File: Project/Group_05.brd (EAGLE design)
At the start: 100 x 80 mm, 29 parts, among them J1 POWER_JACKPTH_LOCK, U1 +12v, U3 TCA9546A_SMD

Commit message: commit
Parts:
- moved D1 144.8 mm to (91.4, 14.0)
- moved R1 142.0 mm to (96.5, 10.2), turned to 90 degrees
- moved J6 130.6 mm to (96.5, 62.2), turned to 270 degrees
- moved J8 126.5 mm to (54.6, 3.81), turned to 90 degrees
- moved U$3 121.4 mm to (71.1, 43.2), turned to 90 degrees
- moved U$2 101.7 mm to (74.9, 2.54)
- moved U3 100.1 mm to (48.3, 57.1)
- moved R10 84.7 mm to (26.7, 11.4)
- moved C2 84.4 mm to (30.5, 69.8)
- moved U2 77.3 mm to (12.7, 11.4)
- moved C1 76.1 mm to (34.3, 74.9)
- moved J7 74.8 mm to (26.7, 77.5)
- moved J1 72.4 mm to (52.1, 26.7)
- moved C3 68.7 mm to (20.3, 74.9)
- moved R4 67.8 mm to (2.54, 35.6)
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
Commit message: Board commit
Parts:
- moved C1 80.7 mm to (72.4, 3.81), turned to 270 degrees
- moved U1 79.2 mm to (83.8, 19.1), turned to 180 degrees
- moved J8 76.4 mm to (34.3, 77.5), turned to 0 degrees
- moved C2 75.5 mm to (64.8, 2.54), turned to 270 degrees
- moved R1 72.8 mm to (24.1, 17.8), turned to 0 degrees
- moved U$2 72.0 mm to (25.2, 54.6), turned to 90 degrees
- moved D1 65.4 mm to (26.7, 22.9)
- moved C3 49.9 mm to (14.0, 25.4)
- moved J3 49.6 mm to (21.6, 77.5)
- moved J4 48.7 mm to (15.2, 77.5)
- moved J2 47.8 mm to (27.9, 77.5)
- moved J6 46.6 mm to (73.7, 21.6), turned to 180 degrees
- moved R11 40.9 mm to (38.1, 22.9), turned to 90 degrees
- moved U3 37.8 mm to (15.0, 39.3), turned to 180 degrees
- moved R2 36.8 mm to (3.81, 35.6), turned to 180 degrees
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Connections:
- removed net MUX_A0/2.3C: U$3.24
- removed net MUX_A1/2.3C: U$3.23
- removed net MUX_A2/2.3C: U$3.22
- removed net MUX_OUT/2.5C: U$3.21
- removed net N$10: R6.1, U3.12
- net I2C_SCL_3: now also R6.1, U3.12
- net MUX_A0/1.3C: now also U$3.24
- net MUX_A1/1.4C: now also U$3.23
- net MUX_A2/1.4C: now also U$3.22
- net MUX_OUT/1.4C: now also U$3.21
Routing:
- net 5V: track 0.00 -> 298.9 mm, vias 0 -> 7
- net I2C_SDA: track 0.00 -> 152.0 mm, vias 0 -> 1
- net I2C_SCL: track 0.00 -> 147.7 mm, vias 0 -> 2
- net GND: track 0.00 -> 146.8 mm, vias 0 -> 2
- net I2C_A2: track 0.00 -> 95.9 mm, vias 0 -> 2
- net I2C_SCL_2: track 0.00 -> 86.2 mm, vias 0 -> 3
- net I2C_SDA_0: track 0.00 -> 69.0 mm
- net MUX_A2/1.4C: track 0.00 -> 66.9 mm, vias 0 -> 3
- net I2C_A0: track 0.00 -> 66.6 mm, vias 0 -> 1
- net I2C_SCL_0: track 0.00 -> 64.1 mm, vias 0 -> 3
- net I2C_SCL_1: track 0.00 -> 62.9 mm
- net I2C_A1: track 0.00 -> 59.9 mm, vias 0 -> 1
- net S1: track 0.00 -> 56.4 mm
- net S2: track 0.00 -> 56.1 mm
- net I2C_SDA_1: track 0.00 -> 55.8 mm, vias 0 -> 4
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
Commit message: brd placement
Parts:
- removed U$3: CY8CKIT-059_TARGET_3, CY8KIT-059:CY8CKIT-059_TARGET_3
- added U$1: CY8CKIT-059_TARGET, CY8KIT-059:CY8CKIT-059_TARGET
- moved J7 91.4 mm to (61.0, 5.08), turned to 270 degrees
- moved J4 77.2 mm to (72.3, 25.4)
- moved R5 75.5 mm to (71.1, 20.3), turned to 270 degrees
- moved R4 71.7 mm to (74.9, 20.3), turned to 270 degrees
- moved C3 55.2 mm to (64.8, 3.81), turned to 90 degrees
- moved R7 53.4 mm to (57.1, 48.3), turned to 0 degrees
- moved R6 53.3 mm to (57.1, 50.8), turned to 0 degrees
- moved J5 53.2 mm to (53.3, 48.3), turned to 90 degrees
- moved J1 47.0 mm to (6.35, 1.27)
- moved S1 40.6 mm to (22.9, 11.4), turned to 0 degrees
- moved U1 39.0 mm to (47.0, 6.35), turned to 0 degrees
- moved C2 35.4 mm to (31.8, 15.2), turned to 90 degrees
- moved R3 29.2 mm to (20.3, 55.9)
- moved J3 28.2 mm to (25.4, 49.5), turned to 270 degrees
- moved U3 27.2 mm to (40.6, 48.3), turned to 0 degrees
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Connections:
- net 5V: now also U$1.26, U$1.27; no longer U$3.26, U$3.27
- net GND: now also U$1.25, U$1.28, U$1.52; no longer U$3.25, U$3.28, U$3.52
- net I2C_A0: now also U$1.6; no longer U$3.6
- net I2C_A1: now also U$1.7; no longer U$3.7
- net I2C_A2: now also U$1.8; no longer U$3.8
- net I2C_SCL: now also U$1.16; no longer U$3.16
- net I2C_SDA: now also U$1.15; no longer U$3.15
- net MUX_A0/1.3C: now also U$1.24; no longer U$3.24
- net MUX_A1/1.4C: now also U$1.23; no longer U$3.23
- net MUX_A2/1.4C: now also U$1.22; no longer U$3.22
- net MUX_OUT/1.4C: now also U$1.21; no longer U$3.21
- net N$1: now also U$1.37; no longer U$3.37
- net N$2: now also U$1.51; no longer U$3.51
- net N$5: now also U$1.36; no longer U$3.36
- net N$6: now also U$1.35; no longer U$3.35
- net N$7: now also U$1.34; no longer U$3.34
- net N$8: now also U$1.33; no longer U$3.33
- net N$9: now also U$1.32; no longer U$3.32
- net PHOTO_OUT: now also U$1.44; no longer U$3.44
- net TEMP_OUT: now also U$1.43; no longer U$3.43
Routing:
- net I2C_SDA: track 152.0 -> 22.0 mm
- net I2C_SCL: track 147.7 -> 22.7 mm, vias 2 -> 1
- net 5V: track 298.9 -> 204.8 mm, vias 7 -> 3
- net GND: track 146.8 -> 238.5 mm, vias 2 -> 5
- net I2C_A2: track 95.9 -> 11.7 mm, vias 2 -> 1
- net MUX_A2/1.4C: track 66.9 -> 15.3 mm, vias 3 -> 1
- net I2C_SDA_0: track 69.0 -> 19.6 mm
- net I2C_SCL_1: track 62.9 -> 16.7 mm
- net S1: track 56.4 -> 10.9 mm
- net I2C_SCL_0: track 64.1 -> 19.0 mm, vias 3 -> 0
- net S2: track 56.1 -> 11.2 mm
- net I2C_A0: track 66.6 -> 26.0 mm
- net I2C_SDA_1: track 55.8 -> 17.7 mm, vias 4 -> 0
- net I2C_SCL_3: track 49.9 -> 14.4 mm, vias 4 -> 2
- net I2C_A1: track 59.9 -> 27.2 mm
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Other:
- board size 100 x 80 mm -> 108.9 x 80 mm

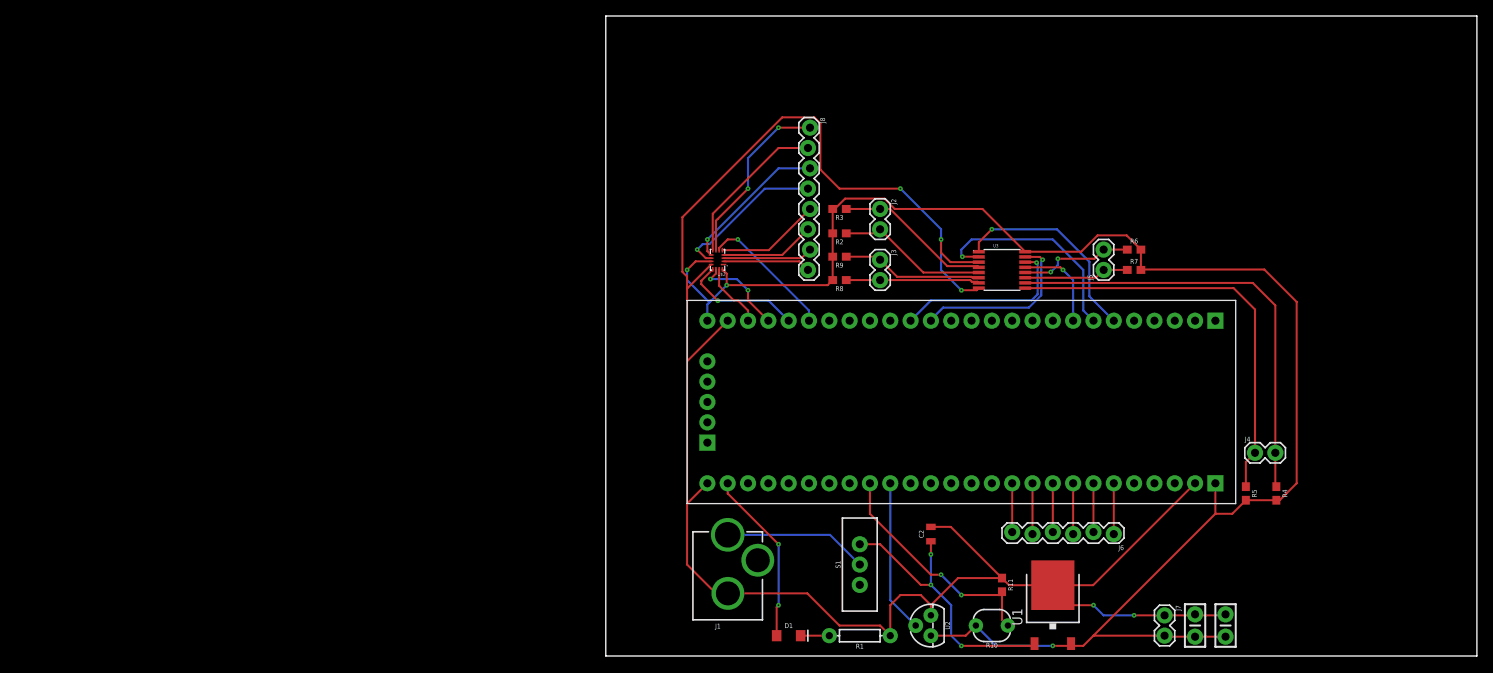
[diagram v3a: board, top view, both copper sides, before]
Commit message: Reduced dimensions
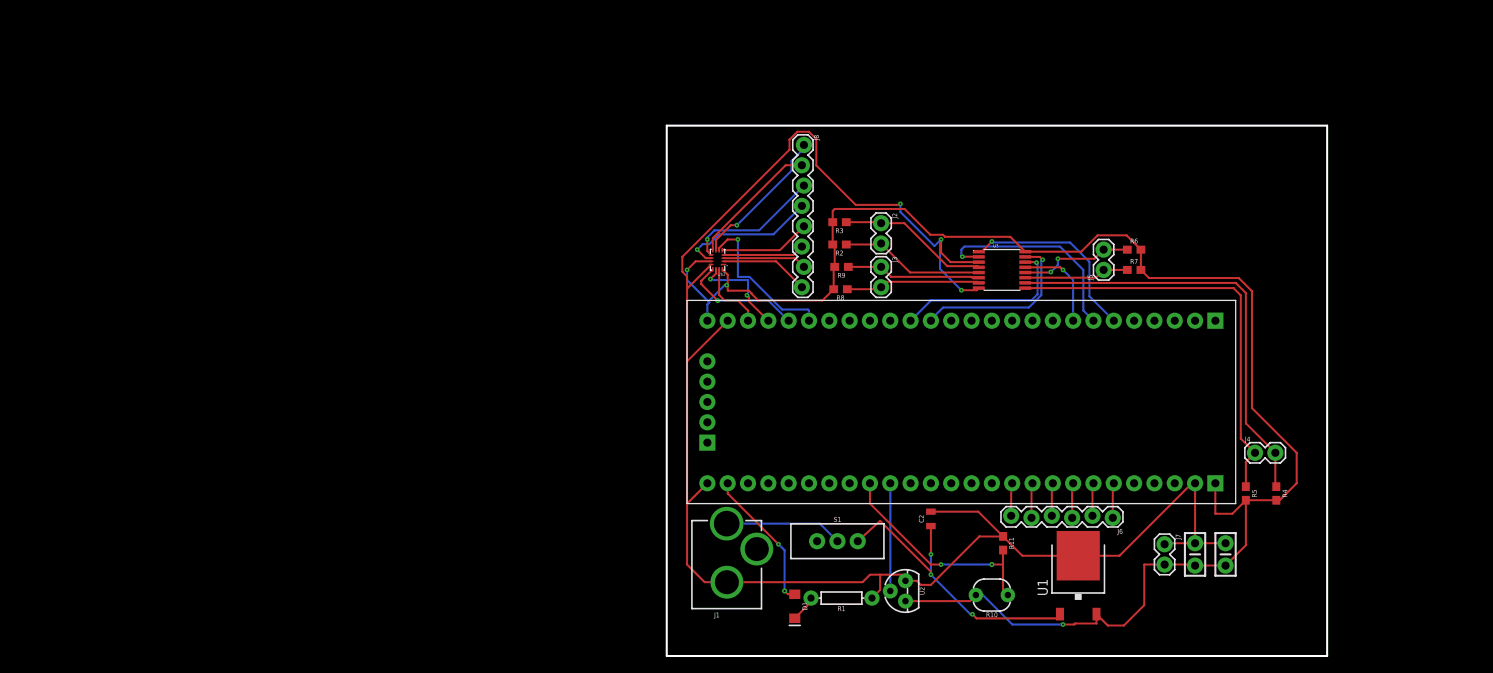
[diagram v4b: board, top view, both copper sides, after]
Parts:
- moved J7 8.89 mm to (61.0, 14.0)
- moved C1 8.89 mm to (68.6, 12.7)
- moved C3 8.89 mm to (64.8, 12.7)
- moved U2 5.36 mm to (28.6, 8.13)
- moved R1 5.23 mm to (20.6, 7.24)
- moved R11 5.21 mm to (40.8, 14.1)
- moved U1 4.86 mm to (50.2, 10.0)
- moved S1 4.04 mm to (20.1, 14.4), turned to 270 degrees
- moved R10 3.81 mm to (39.4, 7.62)
- moved D1 3.76 mm to (14.7, 6.22), turned to 270 degrees
- moved J8 2.29 mm to (15.7, 63.9)
- moved J6 2.04 mm to (54.5, 17.3)
- moved C2 1.90 mm to (31.8, 17.1)
- moved J2 1.78 mm to (25.5, 54.1)
- moved R3 1.65 mm to (20.3, 54.2)
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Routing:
- net GND: track 238.5 -> 224.5 mm, vias 5 -> 3
- net TEMP_OUT: track 19.1 -> 13.5 mm
- net S8: track 22.5 -> 18.2 mm, vias 2 -> 1
- net S7: track 19.9 -> 16.4 mm
- net N$3: track 18.0 -> 14.8 mm
- net N$2: track 21.8 -> 18.5 mm
- net 12V: track 34.9 -> 38.1 mm
- net MUX_OUT/1.4C: track 16.9 -> 19.6 mm
- net 5V: track 204.8 -> 202.5 mm
- net N$1: track 6.10 -> 4.12 mm
- net N$8: track 6.10 -> 4.12 mm
- net N$6: track 6.10 -> 4.12 mm
- net N$9: track 6.35 -> 4.37 mm
- net N$7: track 6.35 -> 4.37 mm
- net N$5: track 6.35 -> 4.37 mm
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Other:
- board size 108.9 x 80 mm -> 82.5 x 66.3 mm

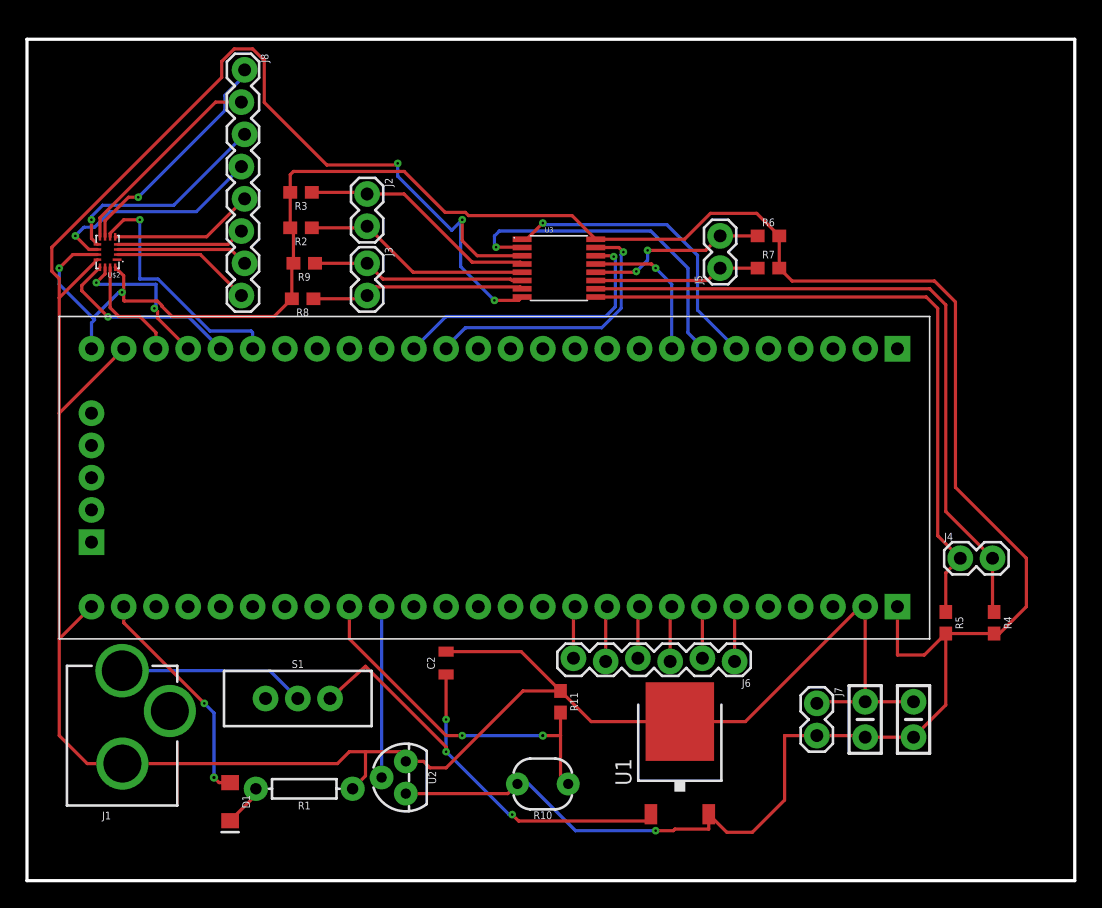
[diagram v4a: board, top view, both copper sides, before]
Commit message: Holes, copper pour
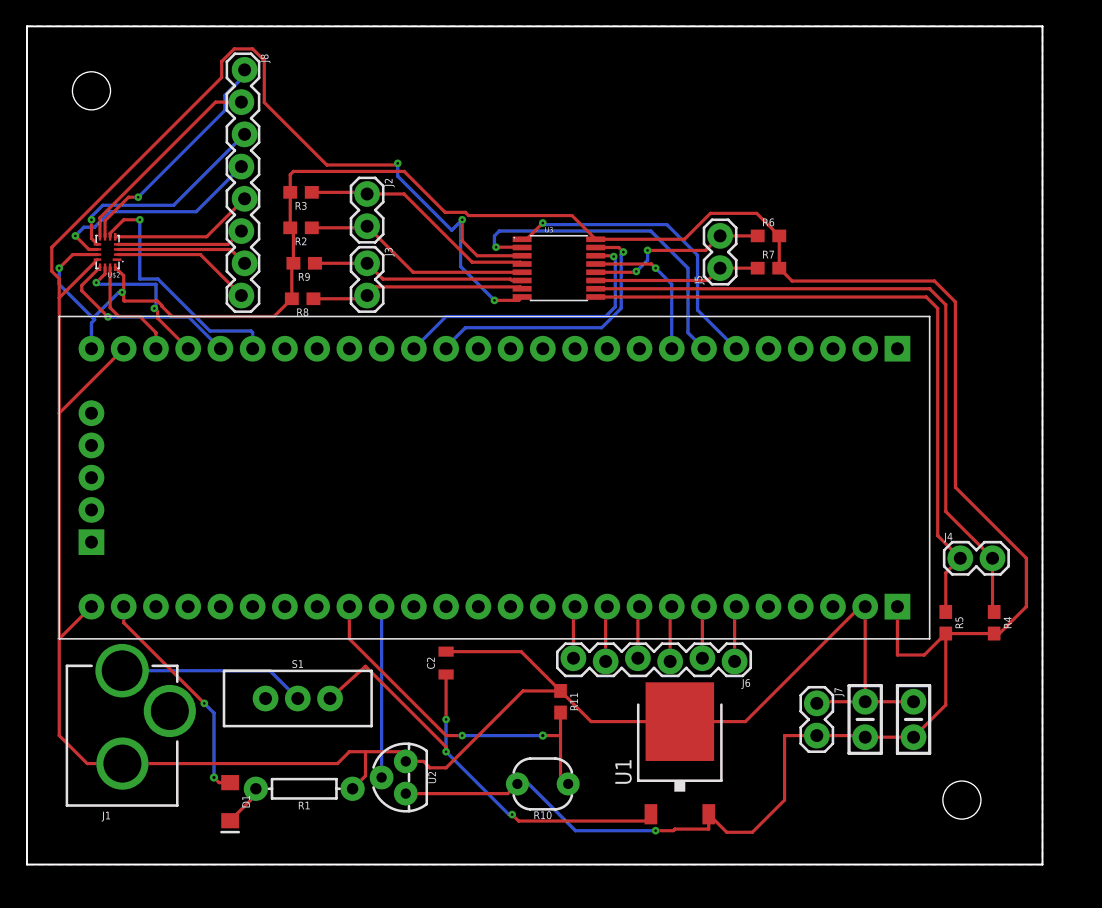
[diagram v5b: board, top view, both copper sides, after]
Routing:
- added copper zone on layer 16, net 5V
- added copper zone on layer 1, net GND
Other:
- board size 82.5 x 66.3 mm -> 80 x 66 mm
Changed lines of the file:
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@@
 <layer number="43" name="vRestrict" color="2" fill="10" visible="yes" active="yes"/>
 <layer number="44" name="Drills" color="7" fill="1" visible="no" active="yes"/>
-<layer number="45" name="Holes" color="7" fill="1" visible="no" active="yes"/>
+<layer number="45" name="Holes" color="7" fill="1" visible="yes" active="yes"/>
 <layer number="46" name="Milling" color="3" fill="1" visible="no" active="yes"/>
 <layer number="47" name="Measures" color="7" fill="1" visible="no" active="yes"/>
@@
 <board>
 <plain>
-<wire x1="-1.27" y1="0" x2="-1.27" y2="66.294" width="0.254" layer="20"/>
-<wire x1="-1.27" y1="66.294" x2="81.28" y2="66.294" width="0.254" layer="20"/>
-<wire x1="81.28" y1="66.294" x2="81.28" y2="0" width="0.254" layer="20"/>
-<wire x1="81.28" y1="0" x2="-1.27" y2="0" width="0.254" layer="20"/>
-<dimension x1="-1.27" y1="0" x2="-1.27" y2="66.294" x3="-6.35" y3="33.147" textsize="1.778" layer="20"/>
-<dimension x1="-1.27" y1="66.294" x2="81.28" y2="66.294" x3="40.005" y3="71.12" textsize="1.778" layer="20"/>
+<hole x="3.81" y="62.23" drill="3"/>
+<hole x="72.39" y="6.35" drill="3"/>
+<wire x1="-1.27" y1="1.27" x2="78.74" y2="1.27" width="0.1524" layer="20"/>
+<wire x1="78.74" y1="1.27" x2="78.74" y2="67.31" width="0.1524" layer="20"/>
+<wire x1="78.74" y1="67.31" x2="-1.27" y2="67.31" width="0.1524" layer="20"/>
+<wire x1="-1.27" y1="67.31" x2="-1.27" y2="1.27" width="0.1524" layer="20"/>
+<dimension x1="-1.27" y1="67.31" x2="-1.27" y2="1.27" x3="-6.35" y3="34.29" textsize="1.778" layer="51"/>
+<dimension x1="78.74" y1="67.31" x2="-1.27" y2="67.31" x3="38.735" y3="73.66" textsize="1.778" layer="51"/>
 </plain>
 <attributes>
@@
 <wire x1="24.384" y1="7.239" x2="25.4" y2="8.255" width="0.254" layer="1"/>
 <wire x1="25.4" y1="8.255" x2="25.4" y2="10.16" width="0.254" layer="1"/>
+<polygon width="0.1524" layer="1" isolate="0.2032">
+<vertex x="-1.27" y="1.27"/>
+<vertex x="-1.27" y="67.31"/>
+<vertex x="78.74" y="67.31"/>
+<vertex x="78.74" y="1.27"/>
+</polygon>
 </signal>
 <signal name="N$3">
@@
 <wire x1="48.26" y1="3.937" x2="49.651" y2="3.937" width="0.254" layer="1"/>
 <wire x1="49.651" y1="3.937" x2="49.778" y2="4.064" width="0.254" layer="1"/>
+<polygon width="0.1524" layer="16" isolate="0.2032">
+<vertex x="-1.27" y="1.27"/>
+<vertex x="-1.27" y="67.31"/>
+<vertex x="78.74" y="67.31"/>
+<vertex x="78.74" y="1.27"/>
+</polygon>
 </signal>
 <signal name="PHOTO_OUT">

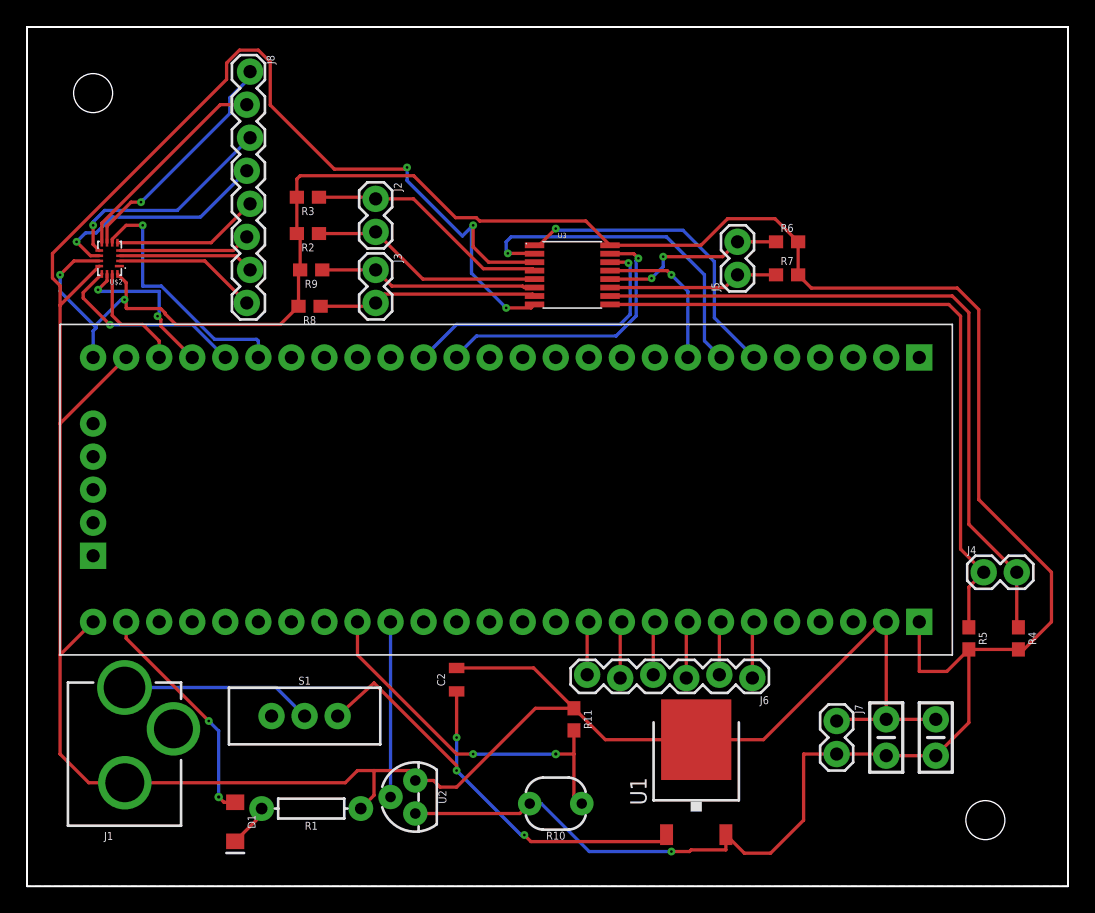
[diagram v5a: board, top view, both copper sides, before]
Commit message: Silkscreen and trace resize
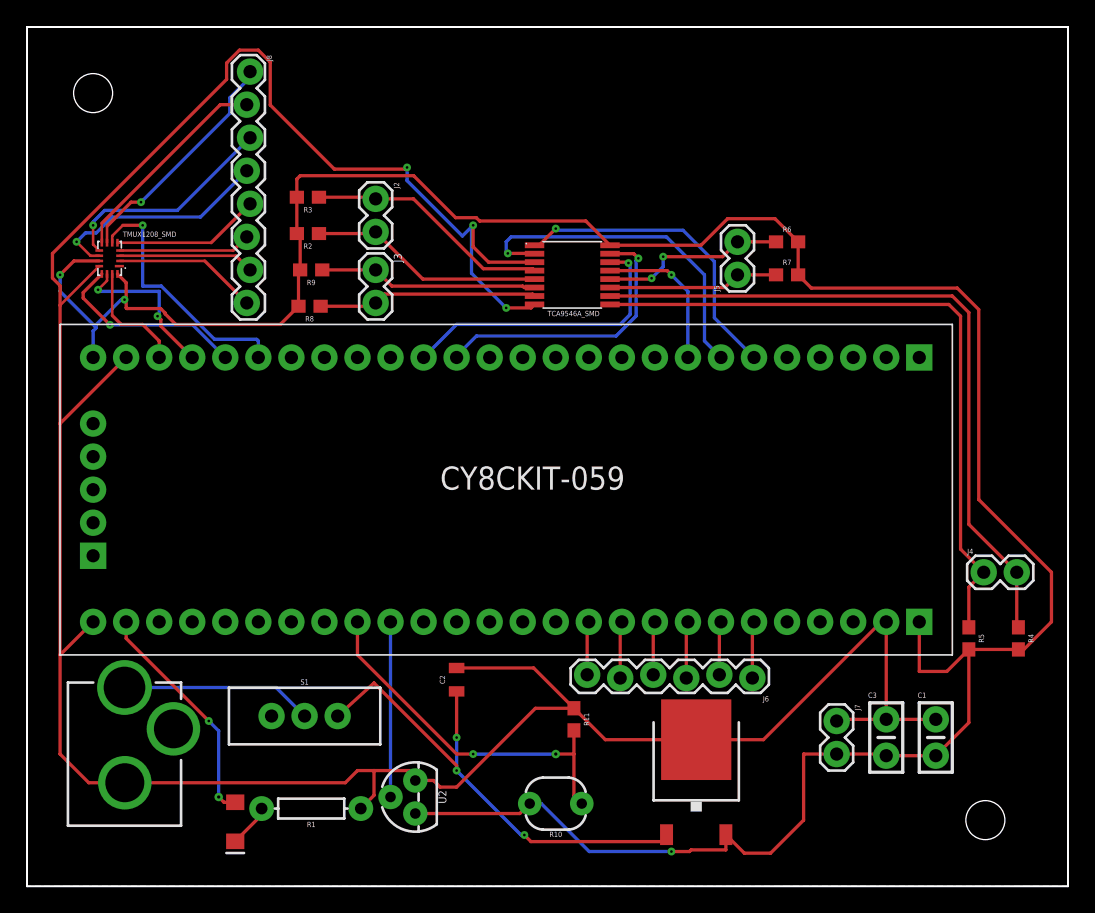
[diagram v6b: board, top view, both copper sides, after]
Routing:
- net GND: track 224.5 -> 220.6 mm
- net N$2: track 18.5 -> 17.8 mm
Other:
- board text added: "0.1µF"
- board text added: "C1"
- board text added: "C3"
- board text added: "CY8CKIT-059"
- board text added: "TCA9546A_SMD"
- board text added: "TMUX1208_SMD"
